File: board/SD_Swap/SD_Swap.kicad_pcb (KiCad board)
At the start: 4 copper layers, 32 x 27 mm, 46 parts, among them J1 USB_C, Q1 Q_Dual_PNP_PNP_E1B1C2E2B2C1, U1 74LVC2G14, U2 RTS5306E, U3 PCB_SD, U4 93AAxxAT, U5 TS3A27518ERTW, U6 SD_SOCKET, U7 AP2127N-3.3, Y1 12MHz

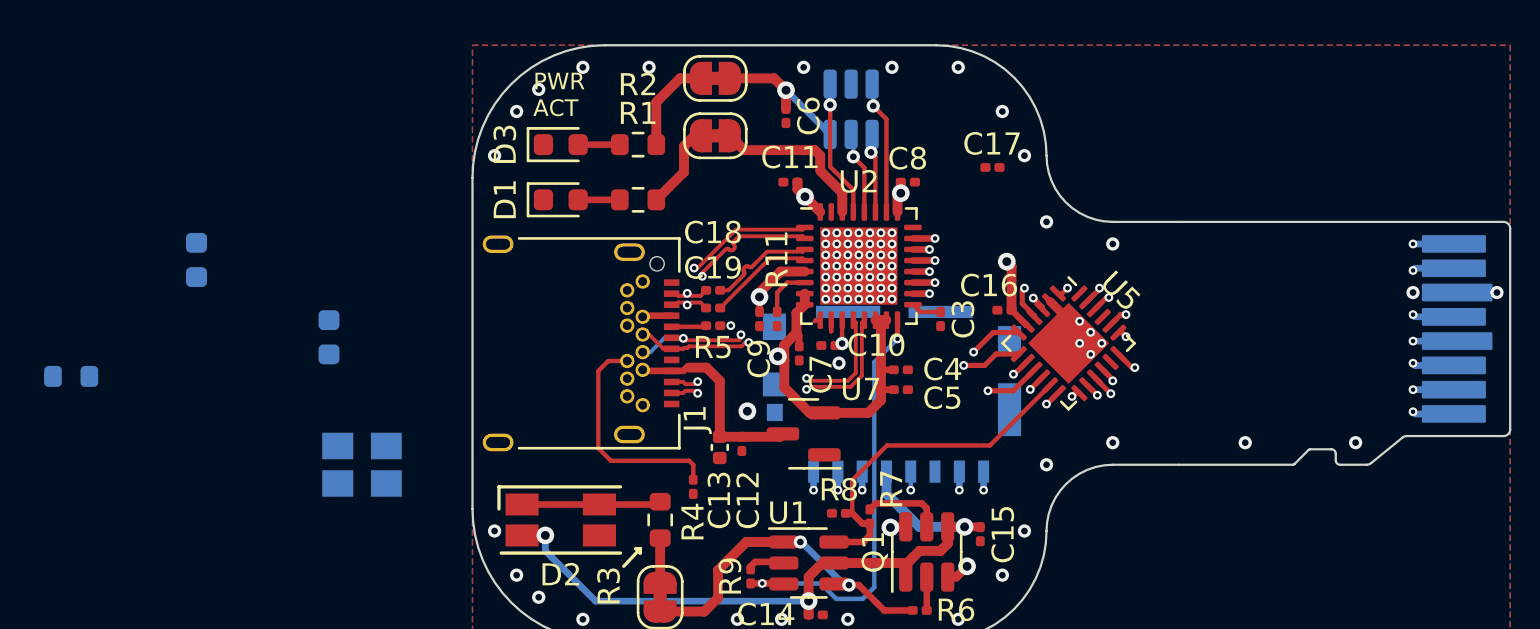
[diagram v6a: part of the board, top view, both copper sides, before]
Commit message: more routing change osc and remove extra cap
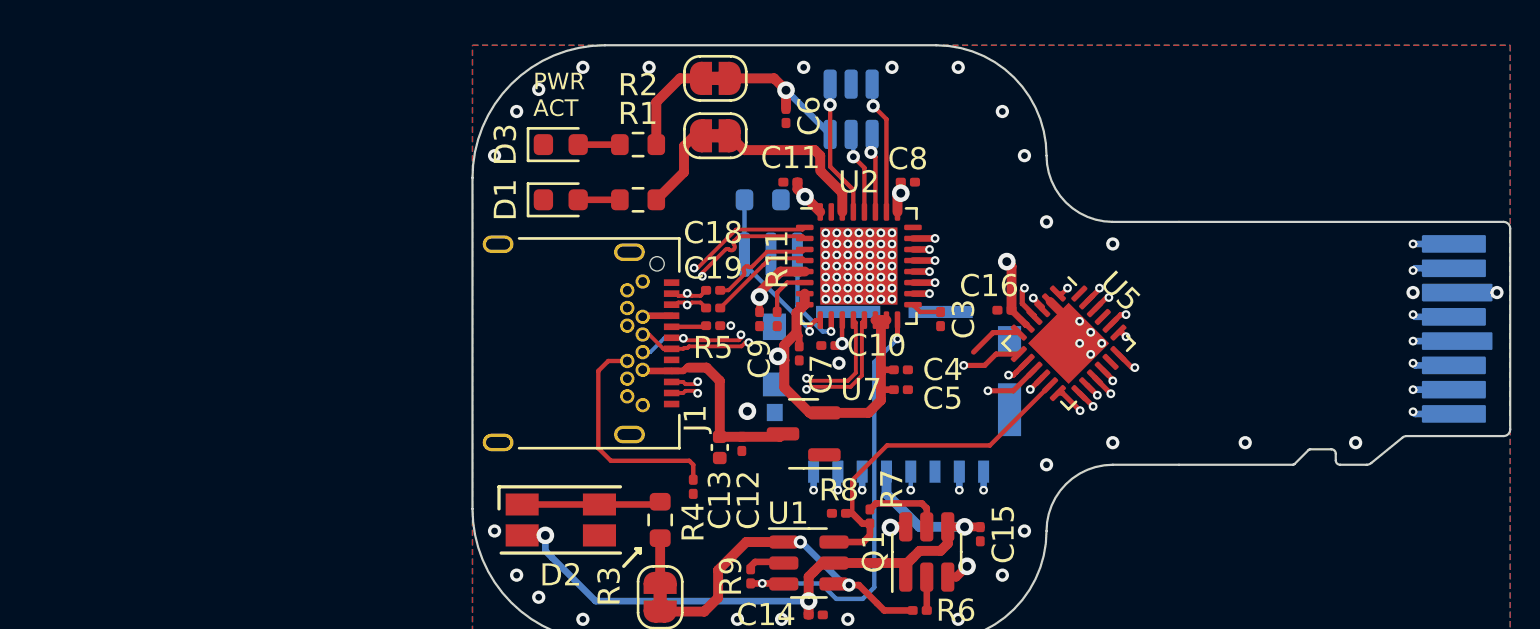
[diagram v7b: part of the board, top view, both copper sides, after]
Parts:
- removed C1, C2: ~20p, Capacitor_SMD:C_0603_1608Metric
- removed C17: 0.1u, Capacitor_SMD:C_0201_0603Metric
- Y1: footprint Crystal:Crystal_SMD_Abracon_ABM8G-4Pin_3.2x2.5mm -> SD_Swap:Resonator-3.2x1.3mm
- moved R10 32.3 mm to (104.1, 75.0), turned to 0 degrees
- moved Y1 19.8 mm to (103.3, 77.5)
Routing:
- net Net-(R10-Pad1): track 0.27 -> 8.01 mm, vias 0 -> 1
- net Net-(U2-Pad18): track 6.89 -> 13.6 mm
- net Net-(U2-Pad10): track 0.52 -> 4.85 mm, vias 0 -> 1
- net Net-(U2-Pad19): track 8.51 -> 12.8 mm
- net Net-(U2-Pad20): track 10.1 -> 12.9 mm
- net Net-(U2-Pad21): track 10.5 -> 12.9 mm
- net Net-(U2-Pad22): track 11.7 -> 12.8 mm
- net Net-(U5-Pad6): vias 2 -> 1

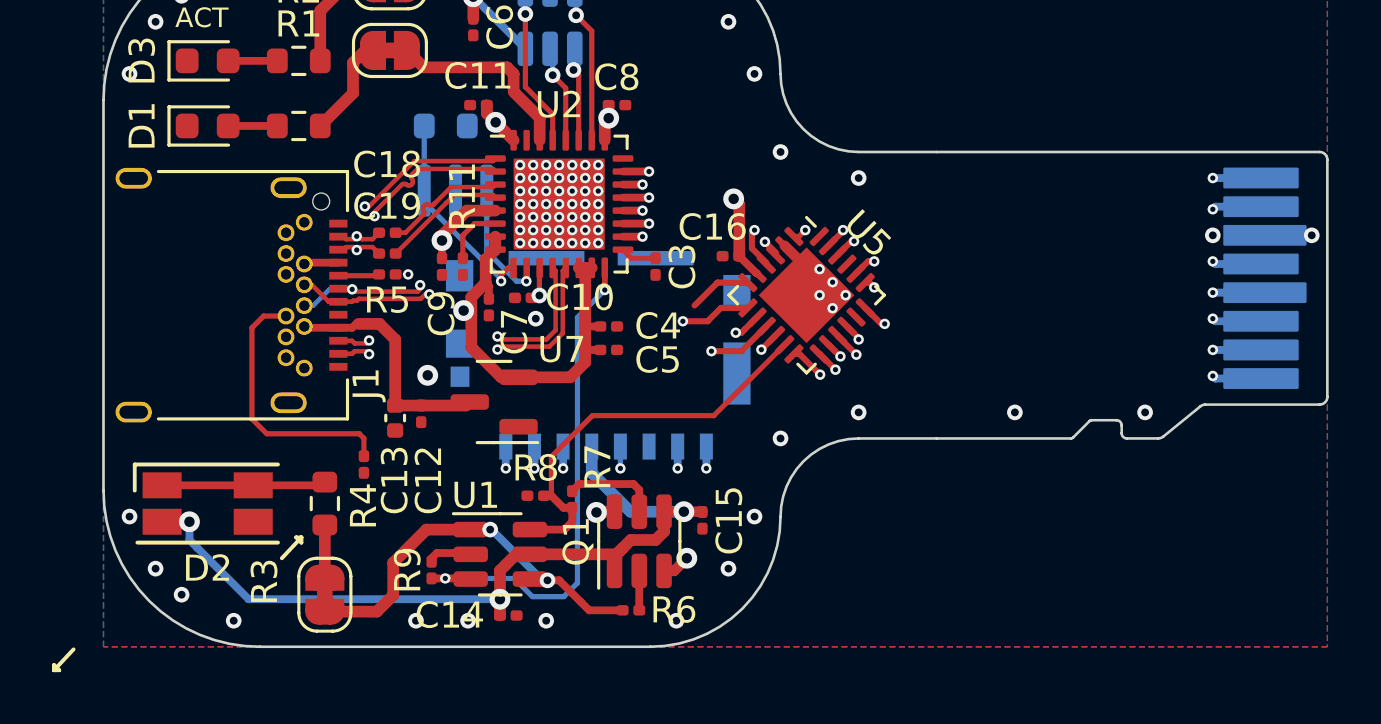
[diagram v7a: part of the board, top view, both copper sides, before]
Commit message: done with routing
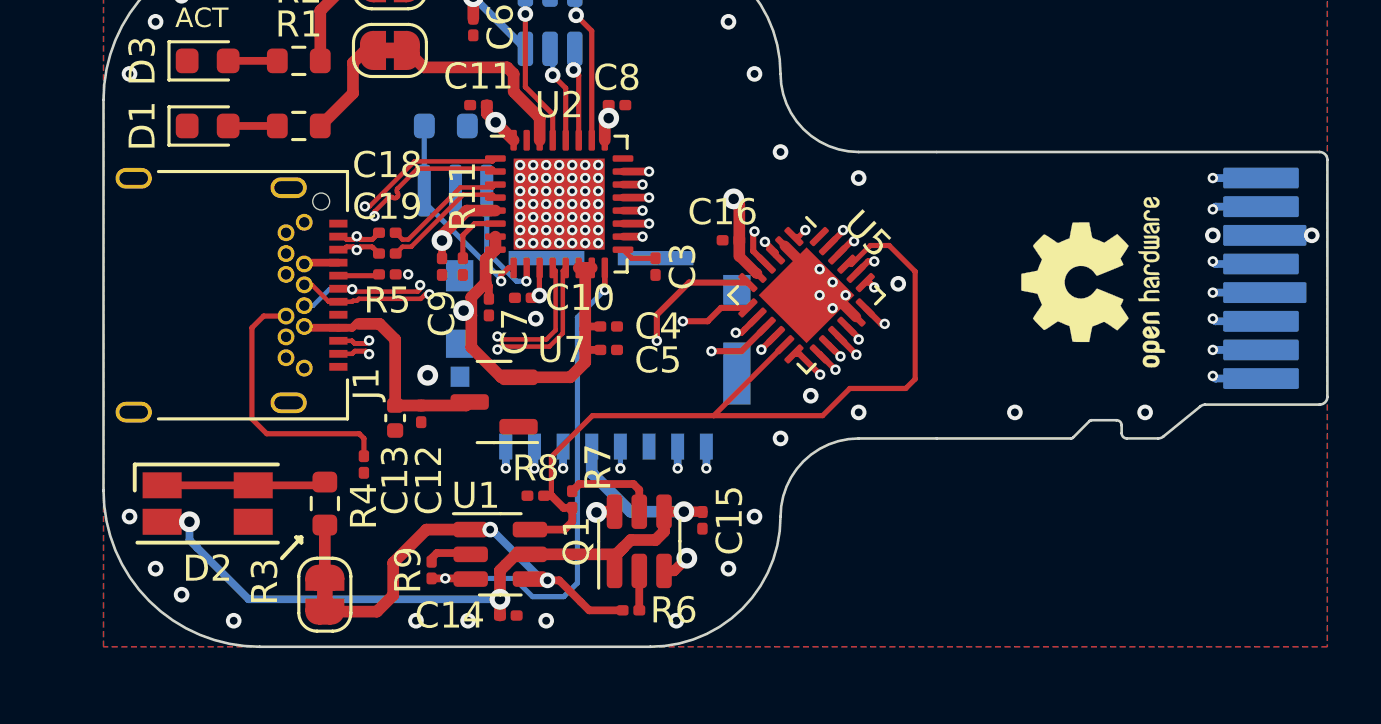
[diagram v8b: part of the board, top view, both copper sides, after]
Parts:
- added REF**: OSHW-Logo2_7.3x6mm_SilkScreen, Symbol:OSHW-Logo2_7.3x6mm_SilkScreen, F.Cu at (129.0, 81.0)
- moved C16 0.61 mm to (115.1, 79.4)
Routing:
- net /SD_SEL: track 15.8 -> 31.6 mm
- net Net-(U5-Pad3): track 12.3 -> 15.9 mm
- net Net-(U5-Pad4): track 16.3 -> 13.6 mm
- net Net-(U5-Pad9): track 10.9 -> 13.5 mm
- net GND: track 3.99 -> 6.23 mm, vias 85 -> 87
- net /SS_TX-: track 8.87 -> 11.0 mm
- net /SS_TX+: track 8.94 -> 11.0 mm
- net Net-(U5-Pad1): track 12.1 -> 13.5 mm
- net Net-(U5-Pad7): track 12.7 -> 13.6 mm
- net Net-(U5-Pad6): track 13.2 -> 13.6 mm, vias 1 -> 2
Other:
- board text removed: "Need to redo usb3 spacing is wrong Length mathicng on sdio"
